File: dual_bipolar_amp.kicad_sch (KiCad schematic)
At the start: 13 parts

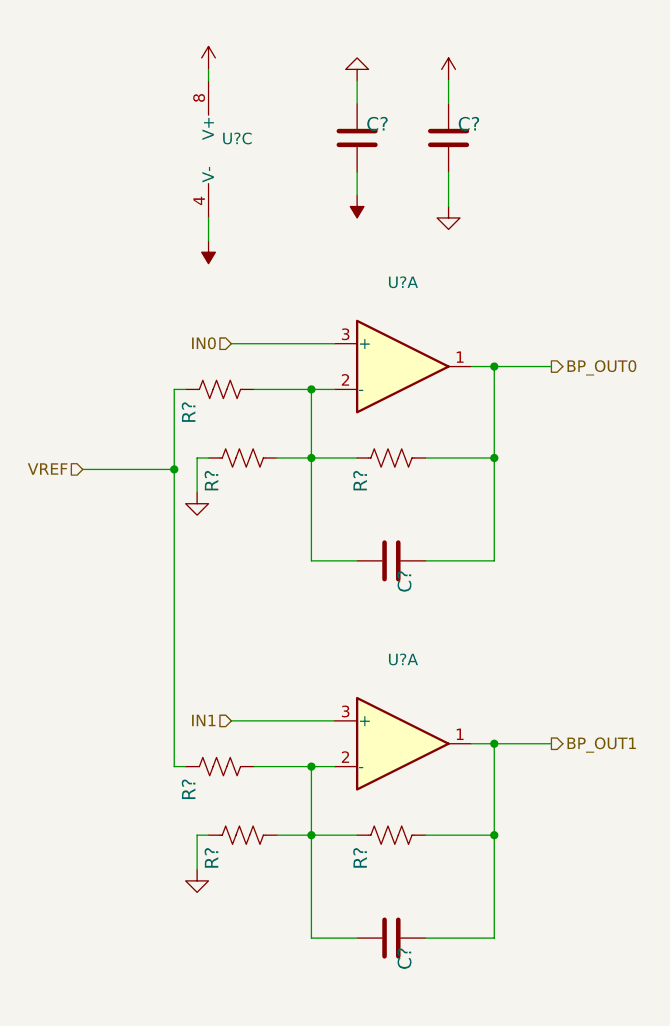
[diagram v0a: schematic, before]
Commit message: closes #31 - incorrect text on Howland current pump. Also, updated fast DAC symbol but not closing until layout is corrected
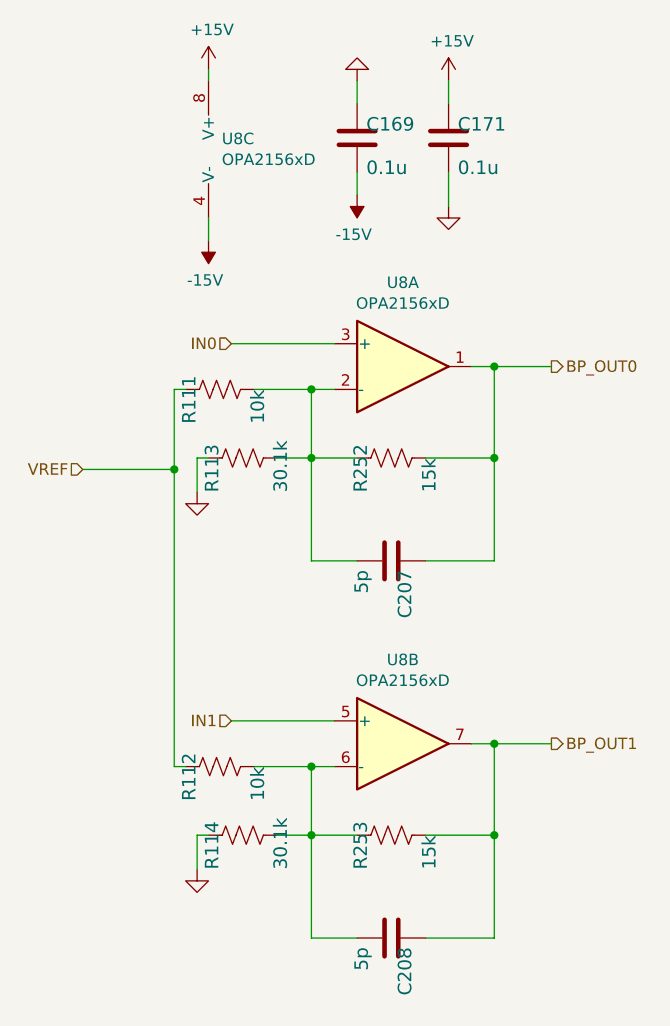
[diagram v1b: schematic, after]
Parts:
- C169, C171: renamed from C?; value (none) -> 0.1u; footprint (none) -> Capacitor_SMD:C_0603_1608Metric
- C207, C208: renamed from C?; value (none) -> 5p; footprint (none) -> Capacitor_SMD:C_0603_1608Metric
- R111, R112: renamed from R?; value (none) -> 10k; footprint (none) -> Resistor_SMD:R_0603_1608Metric
- R113, R114: renamed from R?; value (none) -> 30.1k; footprint (none) -> Resistor_SMD:R_0603_1608Metric
- R252, R253: renamed from R?; value (none) -> 15k; footprint (none) -> Resistor_SMD:R_0603_1608Metric
- U8: renamed from U?; value (none) -> OPA2156xD; footprint (none) -> Package_SO:SOIC-8_3.9x4.9mm_P1.27mm
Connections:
- net BP_OUT1: now also U8.7; no longer U8.1
- net IN1: now also U8.5 (+); no longer U8.3 (+)
- net at C208.2, R112.2, R114.2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: now also U8.6 (-); no longer U8.2 (-)
